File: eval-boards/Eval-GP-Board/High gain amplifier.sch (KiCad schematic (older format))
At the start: 13 parts, among them J6 TP3, J7 TP4, U2 OPA847xD

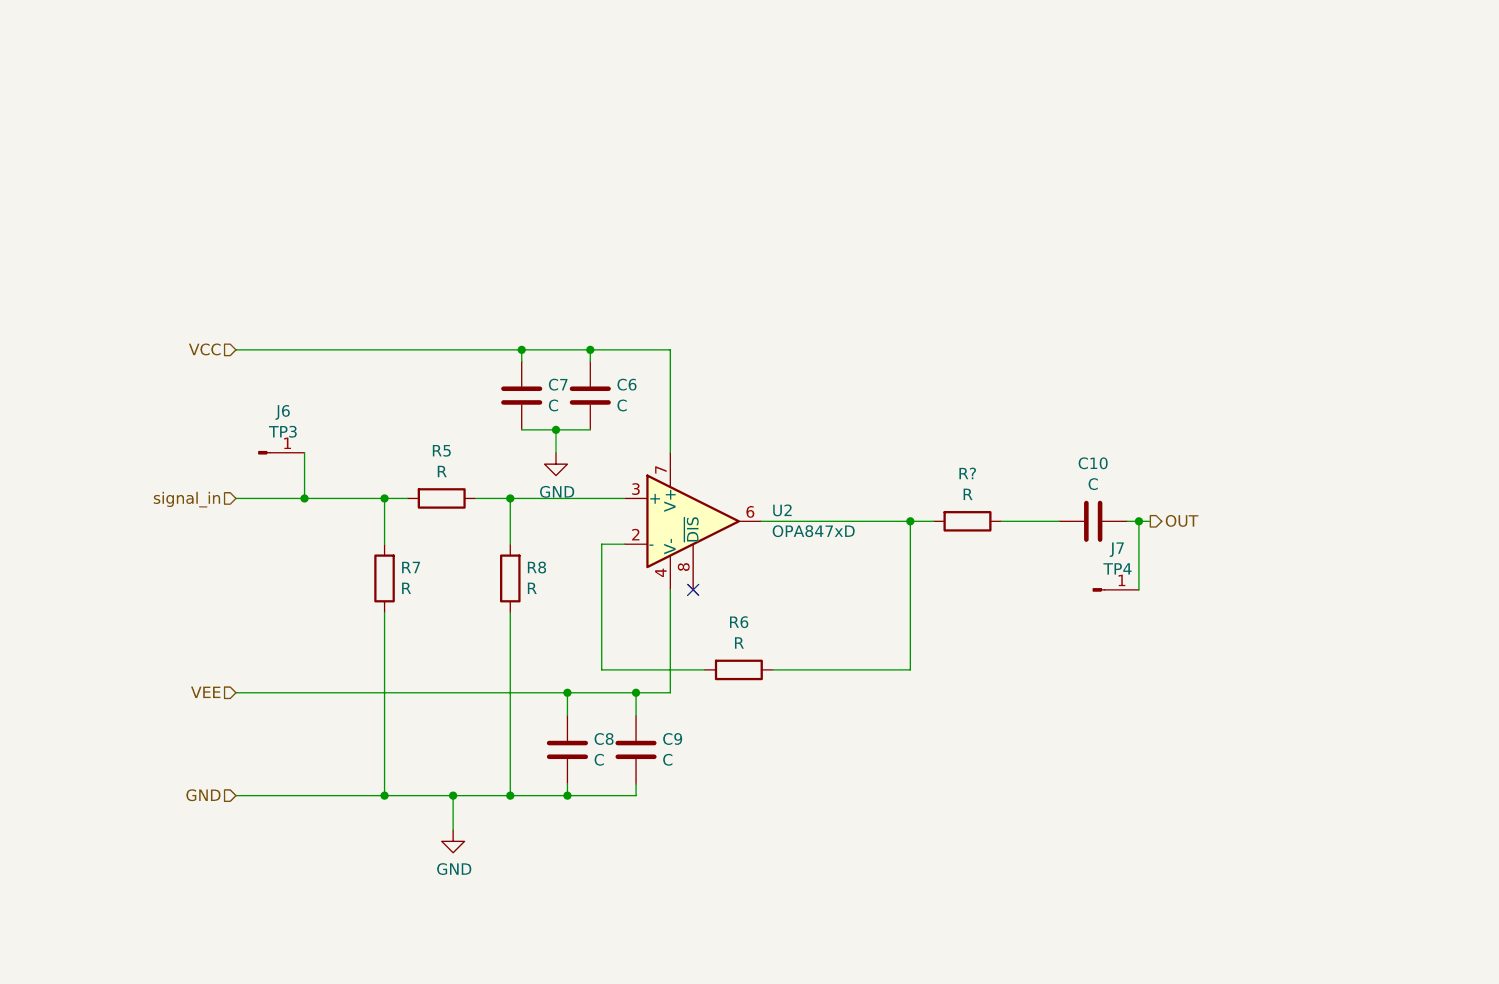
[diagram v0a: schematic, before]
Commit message: Updated schematic
均采用双运放，前级4522可以单运放工作也可以级联工作
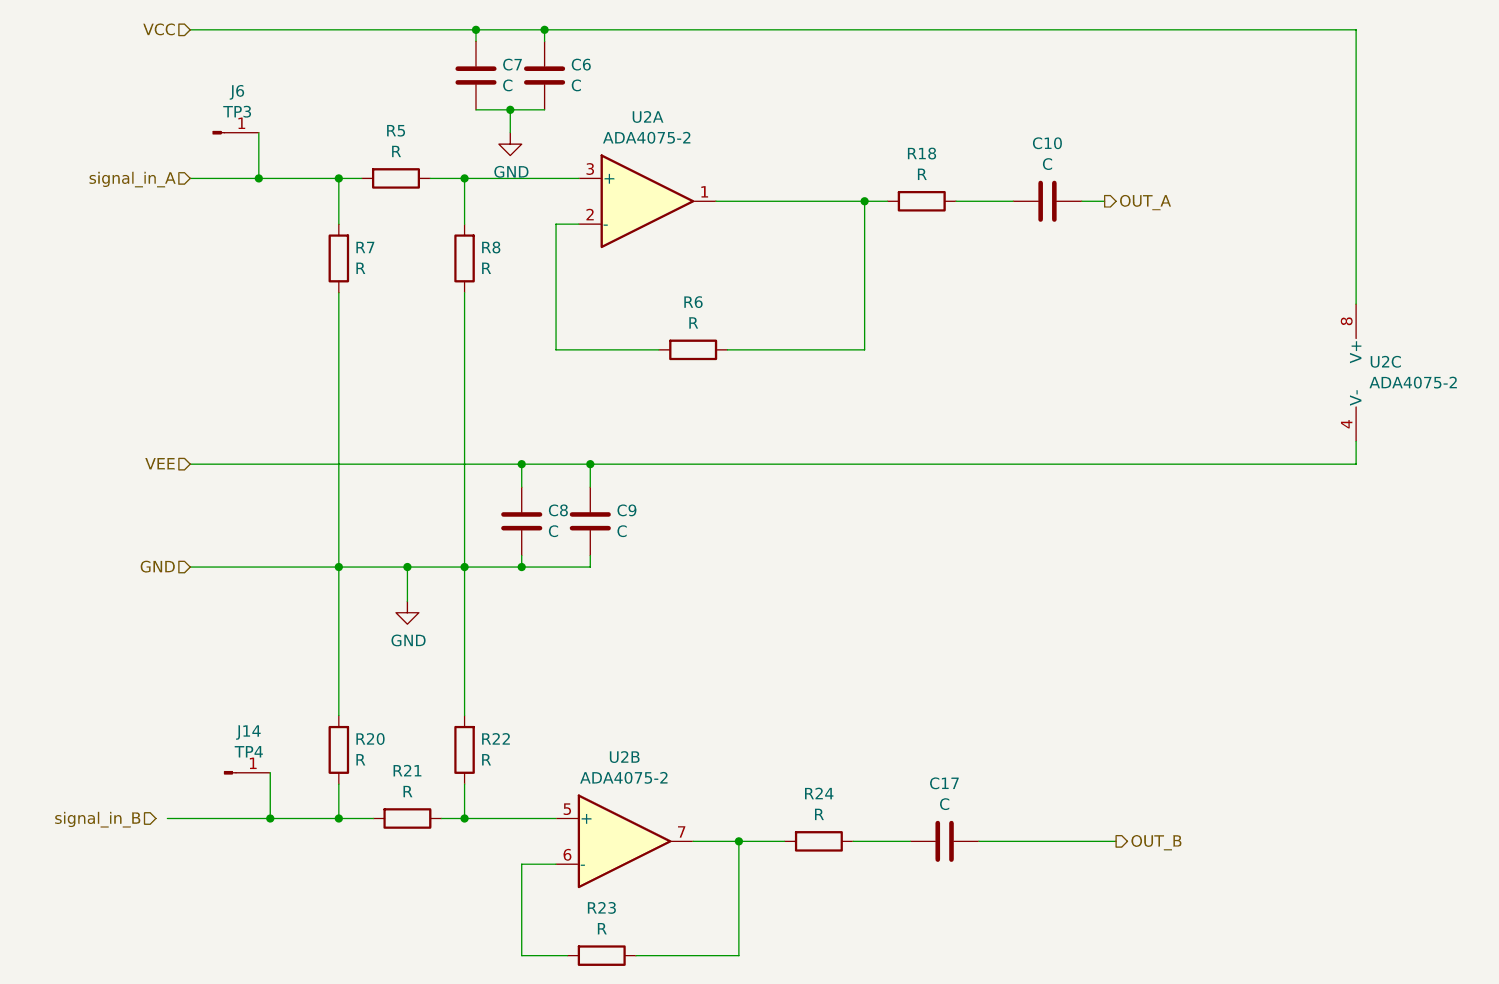
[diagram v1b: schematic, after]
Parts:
- removed J7: TP4, TestPoint:TestPoint_Pad_D2.0mm, symbol Connector:Conn_01x01_Male
- removed U2: OPA847xD, Package_SO:SOIC-8_3.9x4.9mm_P1.27mm, symbol Amplifier_Operational:OPA847xD
- added C17: C, Capacitor_SMD:C_0603_1608Metric, symbol Device:C
- added J14: TP4, TestPoint:TestPoint_Pad_D2.0mm, symbol Connector:Conn_01x01_Male
- added R20, R21, R22, R23, R24: R, Resistor_SMD:R_0603_1608Metric, symbol Device:R
- added U2: ADA4075-2, Package_SO:SOIC-8_3.9x4.9mm_P1.27mm, symbol Amplifier_Operational:ADA4075-2
- gave numbers to parts that had none: 1
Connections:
- net GND: now also R20.2, R22.2
- net VCC: now also U2.8 (V+)
- net VEE: now also U2.4 (V-)
- net at R6.2: now also U2.2 (-)
- net at R5.1, R8.2: now also U2.3 (+)
- net at R18.2, R6.1: now also U2.1
- net OUT renamed OUT_A
- net signal_in renamed signal_in_A
- new net: R21.1, R22.1, U2.5 (+)
- new net: R23.2, U2.6 (-)
- new net: R23.1, R24.2, U2.7
- new net: J14.1 (Pin_1), R20.1, R21.2
- new net: C17.2, R24.1
- new net OUT_B: C17.1
- no-connect marks 1 -> 0
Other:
- moved on the sheet: C10, C6, C7, C8, C9, J6, R18, R5, R6, R7, R8
